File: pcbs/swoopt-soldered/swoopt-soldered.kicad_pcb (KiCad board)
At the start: 2 copper layers, 114 x 97.8 mm, 69 parts, among them J1 TRRS, SW1 MX, SW10 MX, SW11 MX, SW12 MX, SW13 MX, SW14 MX, SW15 MX, SW16 MX, SW17 MX, SW18 MX, SW2 MX, SW3 MX, SW4 MX, SW5 MX, SW6 MX, SW7 MX, SW8 MX, SW9 MX, U1 ProMicro

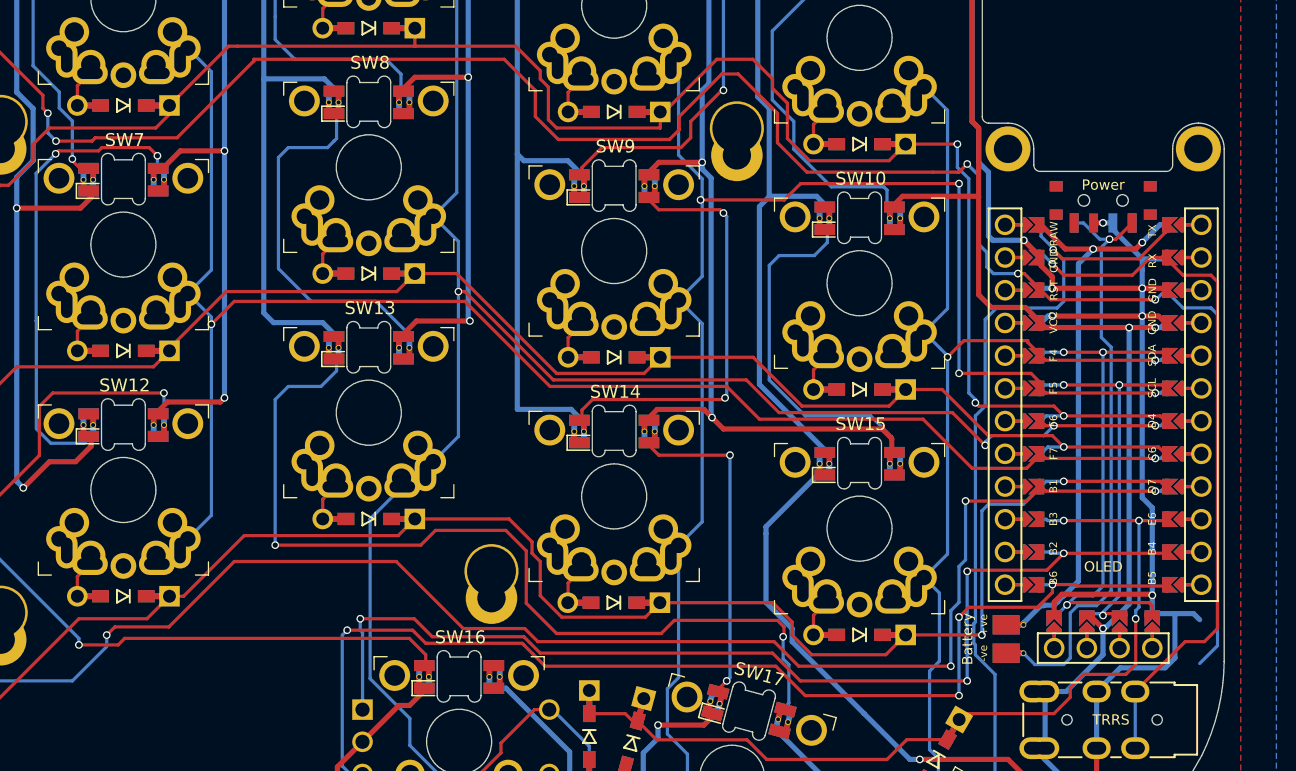
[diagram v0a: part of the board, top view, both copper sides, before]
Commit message: updated footprints and traces. Also added Debora.
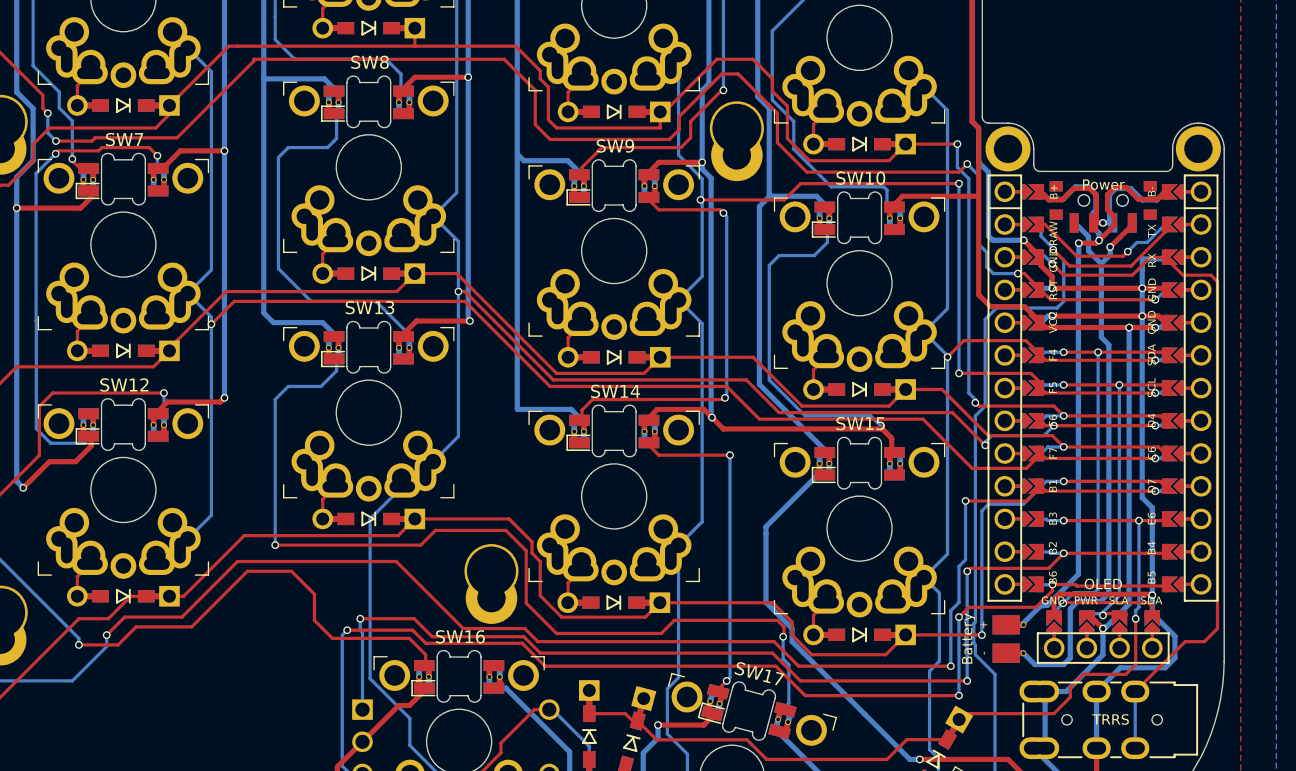
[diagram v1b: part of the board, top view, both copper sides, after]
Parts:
- U1: value ProMicro -> ~; footprint swoop:ProMicro_jumpers -> mcu:U_ProMicro_nRF52840_TH_Reversible
- moved U1 1.29 mm to (166.9, 106.6)
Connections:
- BT1 pad 1: raw -> bat+
- PSW1 pad 2: GND -> bat-
- U1 pad 24: raw -> unconnected-(U1-RAW-Pad24)_1
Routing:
- net bat+: track 0.00 -> 52.0 mm, vias 0 -> 2
- net raw: track 43.2 -> 0.00 mm, vias 2 -> 0
- net reset: track 155.6 -> 123.5 mm
- net bat-: track 0.00 -> 16.9 mm, vias 0 -> 1
- net unconnected-(U1-RAW-Pad24)_1: track 0.00 -> 11.7 mm, vias 0 -> 1
- net GND: track 480.5 -> 472.2 mm, vias 12 -> 11
- net Net-(L1-DOUT): track 83.1 -> 88.6 mm
- net Net-(BT1--): track 45.0 -> 45.6 mm
- net led: track 62.3 -> 62.8 mm
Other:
- board text added: "GND"
- board text added: "PWR"
- board text added: "Power"
- board text added: "SDA"
- board text added: "SLA"
- board text added: "The SWOOPT"

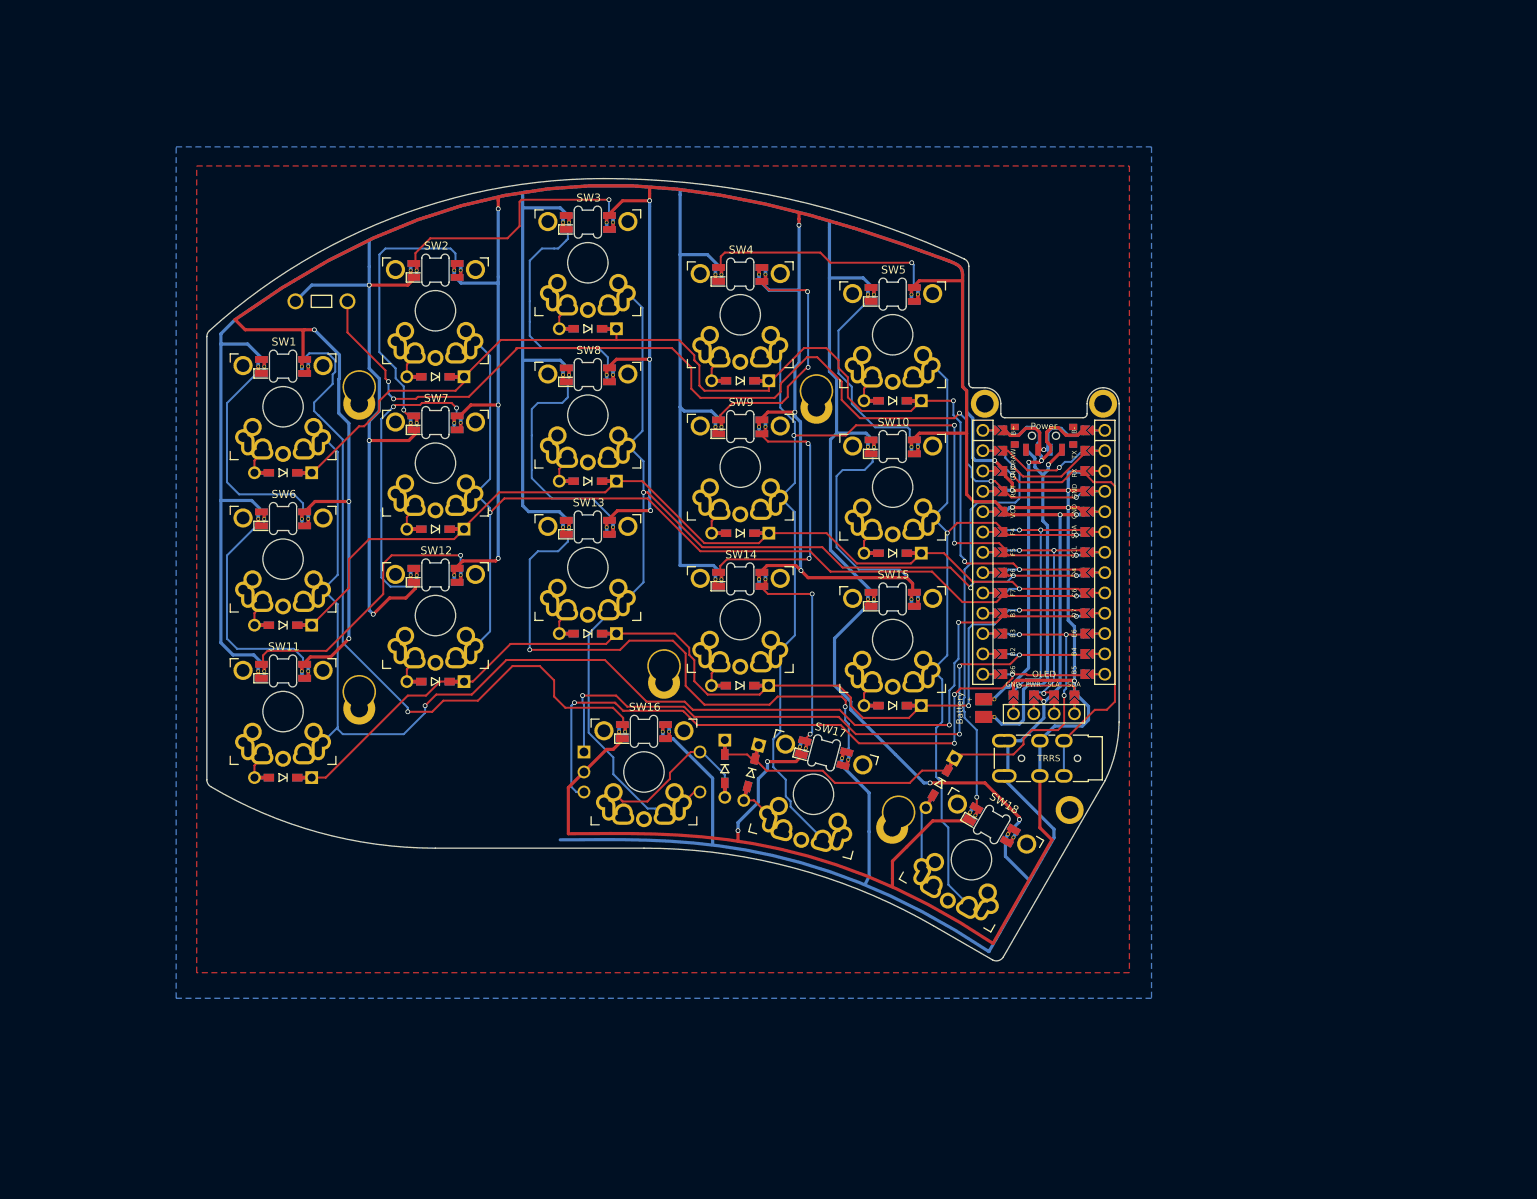
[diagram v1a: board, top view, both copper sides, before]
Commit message: work on the swoopiest - layout defined
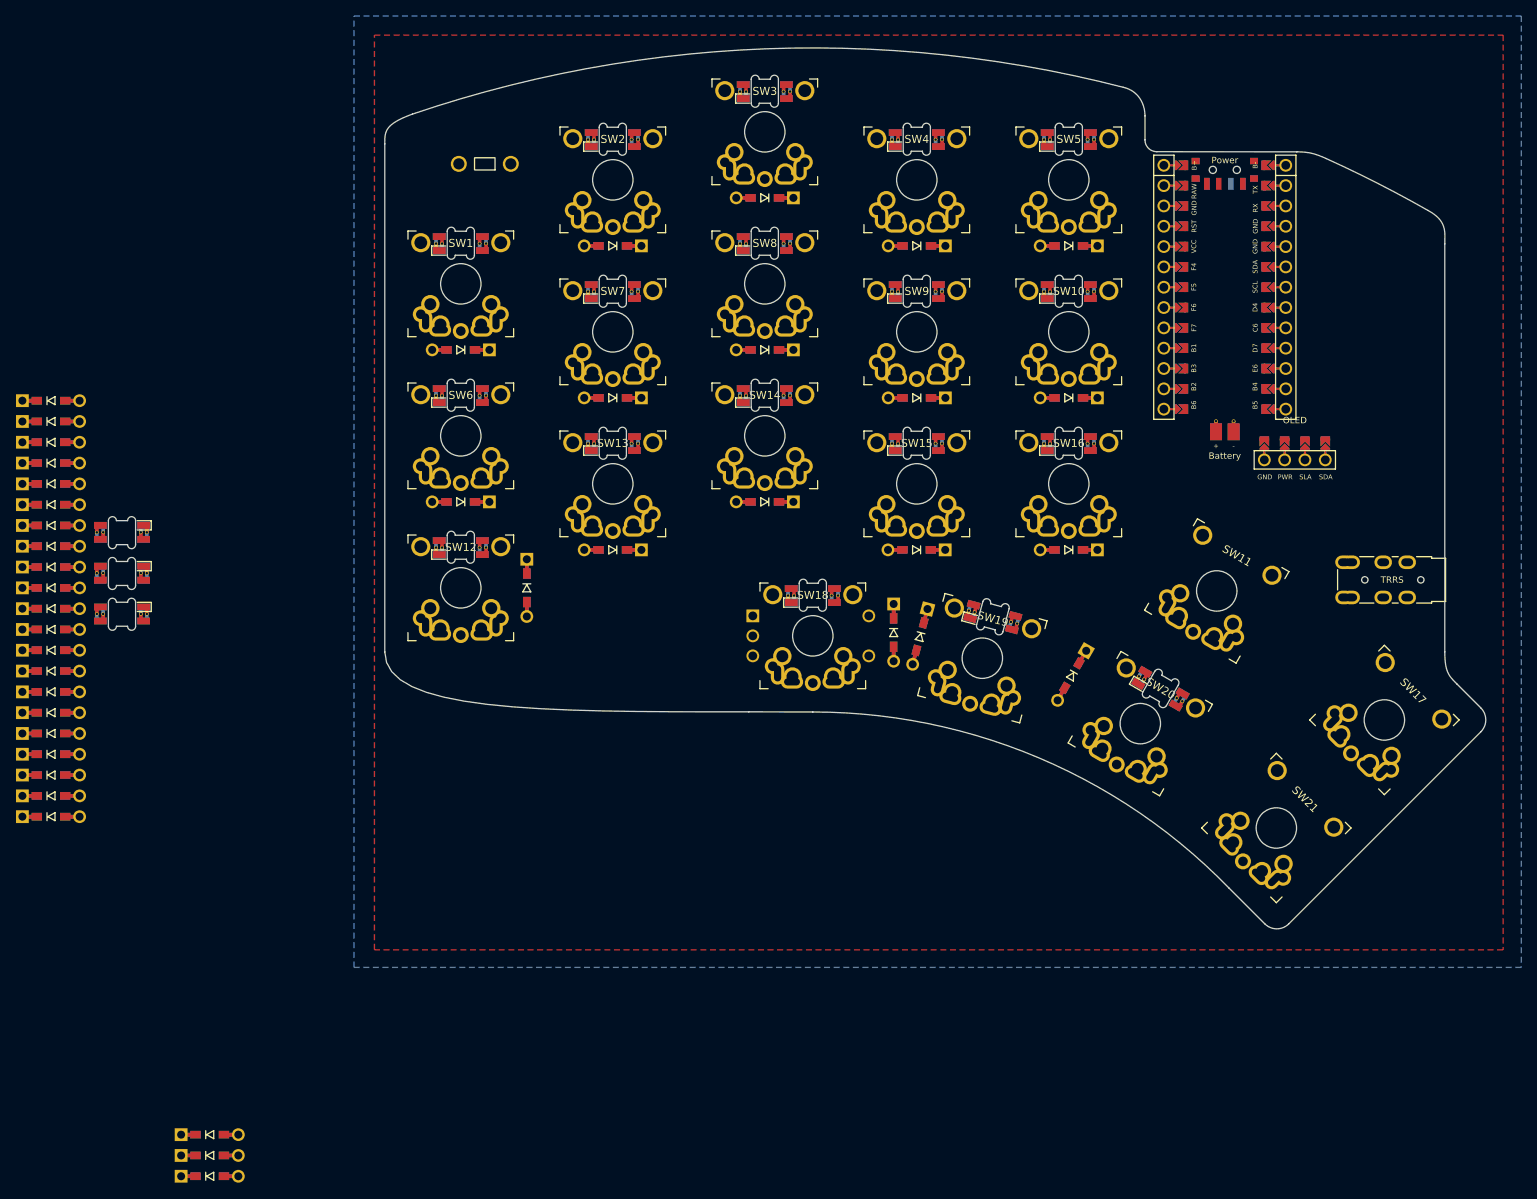
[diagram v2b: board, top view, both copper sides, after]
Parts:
- removed H1, H2, H3, H4 (x2): M2 Hole, swoop:M2_double_hole_4mm
- removed Ref** (x3): Val**, swoop:M2_hole_3.5mm
- added D1: 1N4148, swoop:D_SMD_TH, F.Cu at (42.8, 87.6)
- added D10: 1N4148, swoop:D_SMD_TH, F.Cu at (42.8, 111.0)
- added D11: 1N4148, swoop:D_SMD_TH, F.Cu at (42.8, 113.6)
- added D12: 1N4148, swoop:D_SMD_TH, F.Cu at (42.8, 116.2)
- added D13: 1N4148, swoop:D_SMD_TH, F.Cu at (42.8, 118.8)
- added D14: 1N4148, swoop:D_SMD_TH, F.Cu at (42.8, 121.4)
- added D15: 1N4148, swoop:D_SMD_TH, F.Cu at (42.8, 124.0)
- added D16: 1N4148, swoop:D_SMD_TH, F.Cu at (42.8, 126.6)
- added D17: 1N4148, swoop:D_SMD_TH, F.Cu at (42.8, 129.2)
- added D18: 1N4148, swoop:D_SMD_TH, F.Cu at (42.8, 131.8)
- added D19: 1N4148W, swoop:D_SMD_TH, F.Cu at (62.6, 179.3)
- added D19: 1N4148, swoop:D_SMD_TH, F.Cu at (42.8, 134.4)
- added D2: 1N4148, swoop:D_SMD_TH, F.Cu at (42.8, 90.2)
- added D20: 1N4148W, swoop:D_SMD_TH, F.Cu at (62.6, 181.9)
- added D20: 1N4148, swoop:D_SMD_TH, F.Cu at (42.8, 137.0)
- added D21: 1N4148, swoop:D_SMD_TH, F.Cu at (42.8, 139.6)
- added D21: 1N4148W, swoop:D_SMD_TH, F.Cu at (62.6, 184.5)
- added D3: 1N4148, swoop:D_SMD_TH, F.Cu at (42.8, 92.8)
- added D4: 1N4148, swoop:D_SMD_TH, F.Cu at (42.8, 95.4)
- added D5: 1N4148, swoop:D_SMD_TH, F.Cu at (42.8, 98.0)
- added D6: 1N4148, swoop:D_SMD_TH, F.Cu at (42.8, 100.6)
- added D7: 1N4148, swoop:D_SMD_TH, F.Cu at (42.8, 103.2)
- added D8: 1N4148, swoop:D_SMD_TH, F.Cu at (42.8, 105.8)
- added D9: 1N4148, swoop:D_SMD_TH, F.Cu at (42.8, 108.4)
- added L11: SK6812Mini-e, swoop:SK6812_Mini_E, F.Cu at (51.6, 104.0)
- added L17: SK6812Mini-e, swoop:SK6812_Mini_E, F.Cu at (51.6, 109.1)
- added L21: SK6812Mini-e, swoop:SK6812_Mini_E, F.Cu at (51.6, 114.2)
- added SW11: MX, switches:SW_Universal_TH_Reversible, F.Cu at (188.5, 111.4)
- added SW17: MX, switches:SW_Universal_TH_Reversible, F.Cu at (209.4, 127.5)
- added SW21: MX, switches:SW_Universal_TH_Reversible, F.Cu at (195.9, 141.0)
- SW1, SW10, SW2, SW3, SW4, SW5, SW6, SW7, SW8, SW9: footprint switches:SW_Universal_TH -> switches:SW_Universal_TH_Reversible
- SW12: renamed from SW11; footprint switches:SW_Universal_TH -> switches:SW_Universal_TH_Reversible
- SW13: renamed from SW12; footprint switches:SW_Universal_TH -> switches:SW_Universal_TH_Reversible
- SW14: renamed from SW13; footprint switches:SW_Universal_TH -> switches:SW_Universal_TH_Reversible
- SW15: renamed from SW14; footprint switches:SW_Universal_TH -> switches:SW_Universal_TH_Reversible
- SW16: renamed from SW15; footprint switches:SW_Universal_TH -> switches:SW_Universal_TH_Reversible
- SW18: renamed from SW16; footprint switches:SW_Universal_TH -> switches:SW_Universal_TH_Reversible
- SW19: renamed from SW17; footprint switches:SW_Universal_TH -> switches:SW_Universal_TH_Reversible
- SW20: renamed from SW18; footprint switches:SW_Universal_TH -> switches:SW_Universal_TH_Reversible
- moved J1 48.4 mm to (215.5, 110.0)
- moved BT1 45.8 mm to (189.5, 91.5), turned to 0 degrees
- moved O1 44.6 mm to (194.4, 95.0)
- moved PSW1 40.2 mm to (189.5, 58.8)
- moved U1 40.1 mm to (189.5, 73.4)
- moved D11 38.6 mm to (102.2, 111.0), turned to -90 degrees
- moved D15 29.4 mm to (170.0, 106.2)
- moved SW16 29.4 mm to (170.0, 98.0)
- moved L16 29.4 mm to (170.0, 93.1)
- moved D10 29.4 mm to (170.0, 87.3)
- moved SW10 29.4 mm to (170.0, 79.0)
- moved L10 29.4 mm to (170.0, 74.1)
- moved D5 29.3 mm to (170.0, 68.3)
- moved SW5 29.3 mm to (170.0, 60.0)
- moved L5 29.3 mm to (170.0, 55.1)
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- renumbered L11 to L12, L12 to L13, L13 to L14, L14 to L15, L15 to L16, L16 to L18, L17 to L19, L18 to L20
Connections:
- L20 pad 4: led -> Net-(L20-DIN)
- SW12 pad 2: Net-(D11-A) -> Net-(D12-A)
- SW13 pad 2: Net-(D12-A) -> Net-(D13-A)
- SW14 pad 2: Net-(D13-A) -> Net-(D14-A)
- SW15 pad 2: Net-(D14-A) -> Net-(D15-A)
- SW16 pad 2: Net-(D15-A) -> Net-(D16-A)
- SW19 pad 2: Net-(D17-A) -> Net-(D19-A)
- SW20 pad 2: Net-(D18-A) -> Net-(D20-A)
- U1 pad 15: unconnected-(U1-B3/14-Pad15)_1 -> col5
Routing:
- net GND: track 472.2 -> 0.00 mm, vias 11 -> 0
- net VCC: track 406.4 -> 0.00 mm, vias 15 -> 0
- net col0: track 155.4 -> 0.00 mm, vias 4 -> 0
- net row0: track 140.8 -> 0.00 mm, vias 3 -> 0
- net col2: track 136.8 -> 0.00 mm, vias 4 -> 0
- net reset: track 123.5 -> 0.00 mm, vias 5 -> 0
- net row2: track 123.2 -> 0.00 mm, vias 2 -> 0
- net col1: track 122.1 -> 0.00 mm, vias 2 -> 0
- net col3: track 120.1 -> 0.00 mm, vias 4 -> 0
- net row1: track 115.9 -> 0.00 mm, vias 1 -> 0
- net col4: track 91.2 -> 0.00 mm, vias 2 -> 0
- net Net-(L1-DOUT): track 88.6 -> 0.00 mm, vias 1 -> 0
- net edb: track 86.6 -> 0.00 mm, vias 4 -> 0
- net eda: track 82.6 -> 0.00 mm, vias 4 -> 0
- net Net-(L14-DIN): track 71.0 -> 0.00 mm, vias 2 -> 0
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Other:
- board size 114 x 97.8 mm -> 137.6 x 110.1 mm
- board text added: "The SWOOPIEST"
- board text removed: "The SWOOPT"
